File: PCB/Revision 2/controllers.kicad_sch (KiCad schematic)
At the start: 2 parts

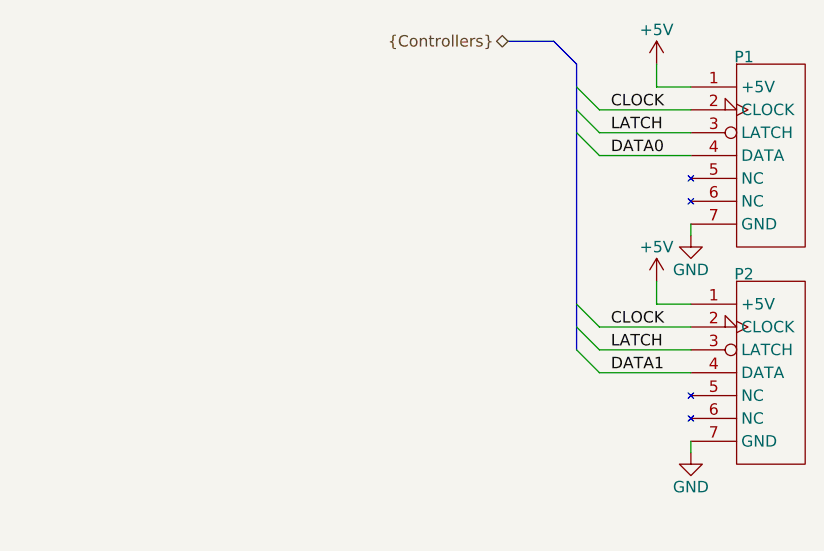
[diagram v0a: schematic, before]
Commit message: ESD protection diodes go BRRRRRRR
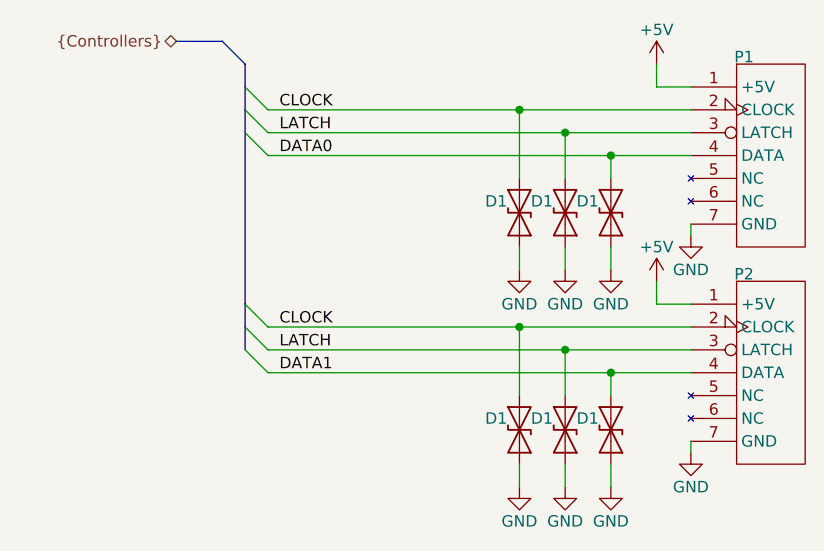
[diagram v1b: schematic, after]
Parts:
- added D1 (x6): ESD9B3.3ST5G, Diode_SMD:D_SOD-923, symbol Diode:ESD9B3.3ST5G
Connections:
- net CLOCK: now also D1.1 (A1), D1.1 (A1)
- net DATA0: now also D1.1 (A1)
- net DATA1: now also D1.1 (A1)
- net GND: now also D1.2 (A2), D1.2 (A2), D1.2 (A2), D1.2 (A2), D1.2 (A2), D1.2 (A2)
- net LATCH: now also D1.1 (A1), D1.1 (A1)
